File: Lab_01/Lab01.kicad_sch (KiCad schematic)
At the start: 0 parts

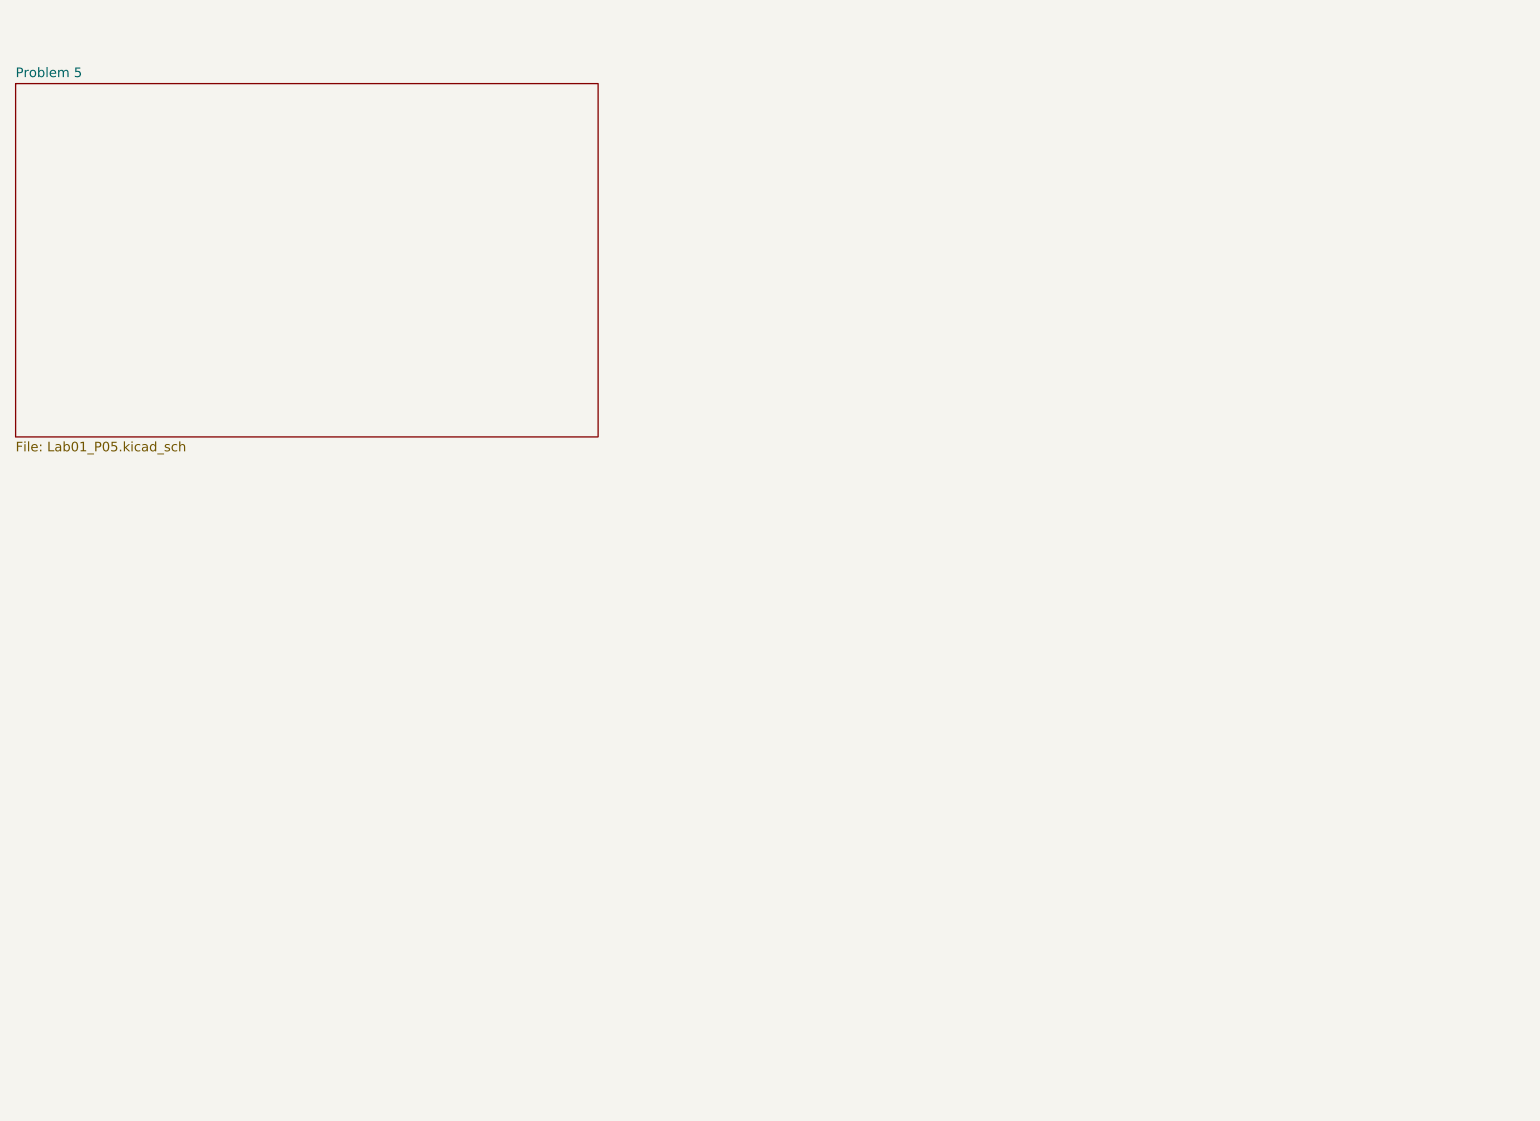
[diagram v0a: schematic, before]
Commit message: Capture and simulate P6&7 schemas
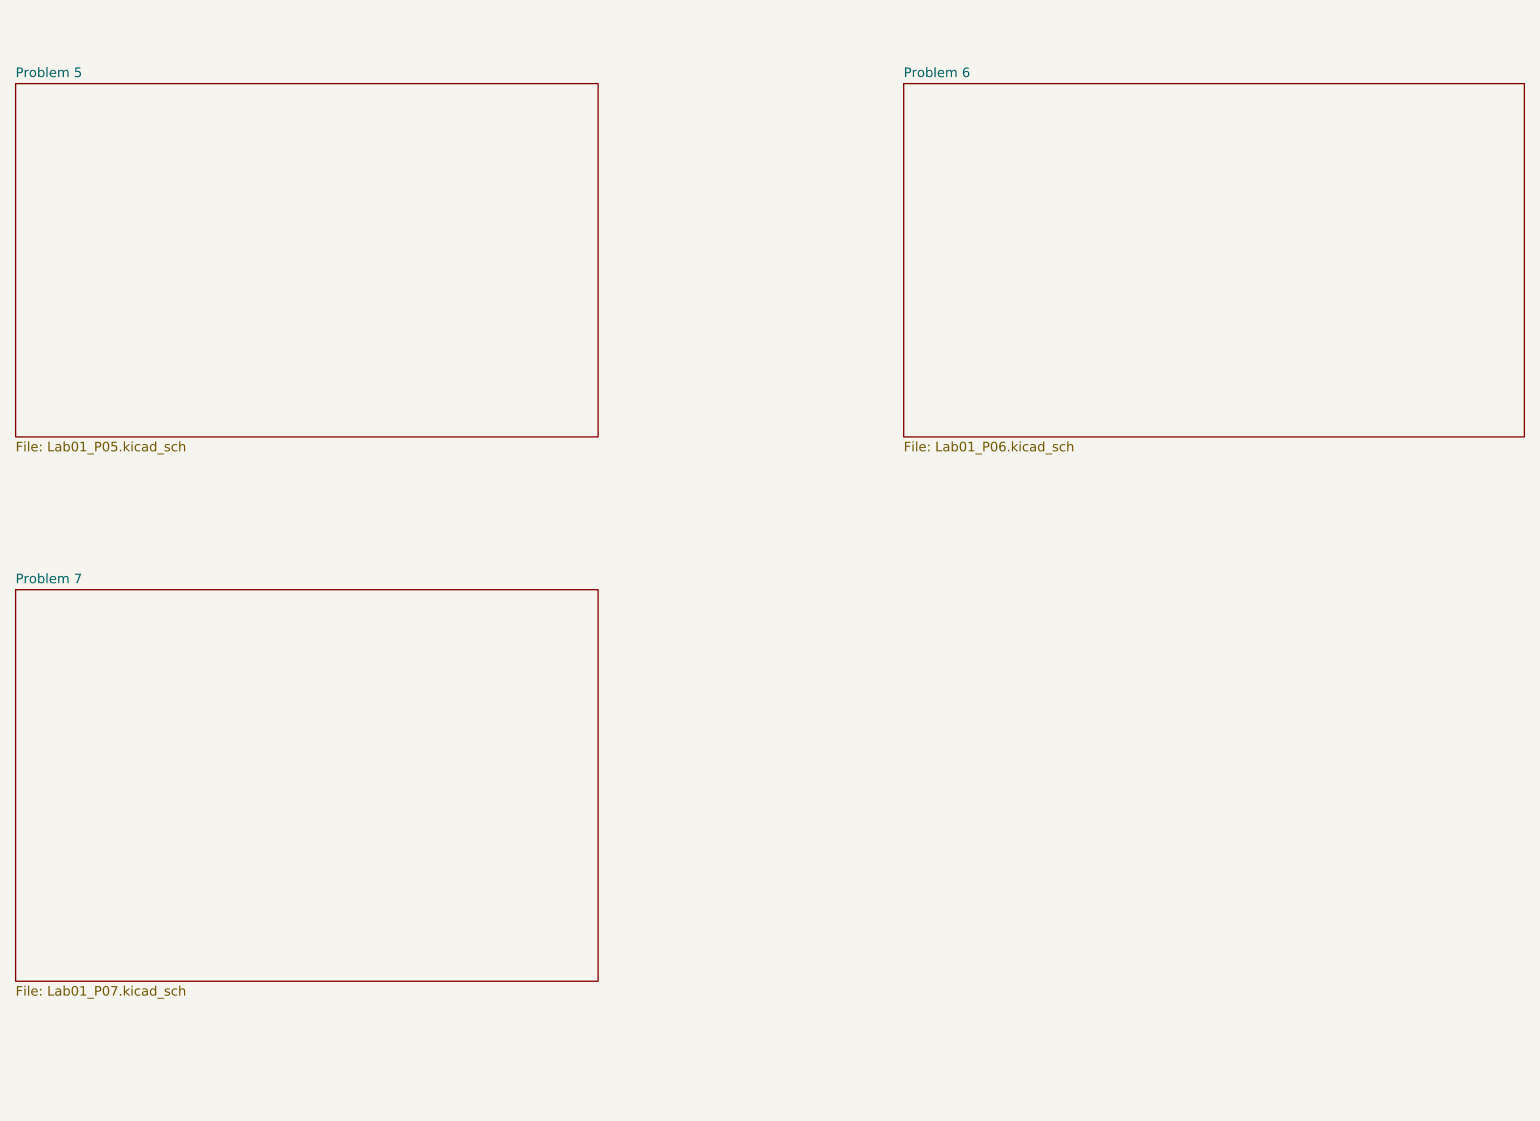
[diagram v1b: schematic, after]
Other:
- added sheet Problem 6 (Lab01_P06.kicad_sch)
- added sheet Problem 7 (Lab01_P07.kicad_sch)
- company: (none) -> Jim Horwitz & Mark Vaughn, Jork Incorporated
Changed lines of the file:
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@@
 (kicad_sch (version 20230121) (generator eeschema)
   (paper "A4")
+  (title_block
+    (date "2024-01-19")
+    (rev "0")
+    (company "Jim Horwitz & Mark Vaughn, Jork Incorporated")
+  )
+  (sheet (at 38.1 99.06) (size 77.47 52.07) (fields_autoplaced)
+    (stroke (width 0.1524) (type solid))
+    (fill (color 0 0 0 0.0000))
+    (property "Sheetname" "Problem 7" (at 38.1 98.3484 0)
+      (effects (font (size 1.27 1.27)) (justify left bottom))
+    )
+    (property "Sheetfile" "Lab01_P07.kicad_sch" (at 38.1 151.7146 0)
+      (effects (font (size 1.27 1.27)) (justify left top))
+    )
+    (instances
+      (project "Lab01"
+        (path "/f5e37932-d66b-45bd-afc2-f24a1a74700d" (page "4"))
+      )
+    )
+  )
   (sheet (at 38.1 31.75) (size 77.47 46.99) (fields_autoplaced)
     (stroke (width 0.1524) (type solid))
@@
       )
     )
+  )
+  (sheet (at 156.21 31.75) (size 82.55 46.99) (fields_autoplaced)
+    (stroke (width 0.1524) (type solid))
+    (fill (color 0 0 0 0.0000))
+    (property "Sheetname" "Problem 6" (at 156.21 31.0384 0)
+      (effects (font (size 1.27 1.27)) (justify left bottom))
+    )
+    (property "Sheetfile" "Lab01_P06.kicad_sch" (at 156.21 79.3246 0)
+      (effects (font (size 1.27 1.27)) (justify left top))
+    )
+    (instances
+      (project "Lab01"
+        (path "/f5e37932-d66b-45bd-afc2-f24a1a74700d" (page "3"))
+      )
+    )

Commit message: Edit up to Question 9
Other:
- added sheet Problem 8 (Lab01_P08.kicad_sch)
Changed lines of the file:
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@@
     (company "Jim Horwitz & Mark Vaughn, Jork Incorporated")
   )
-  (sheet (at 38.1 99.06) (size 77.47 52.07) (fields_autoplaced)
+  (sheet (at 38.1 101.6) (size 38.1 25.4) (fields_autoplaced)
     (stroke (width 0.1524) (type solid))
     (fill (color 0 0 0 0.0000))
-    (property "Sheetname" "Problem 7" (at 38.1 98.3484 0)
+    (property "Sheetname" "Problem 7" (at 38.1 100.8884 0)
       (effects (font (size 1.27 1.27)) (justify left bottom))
     )
-    (property "Sheetfile" "Lab01_P07.kicad_sch" (at 38.1 151.7146 0)
+    (property "Sheetfile" "Lab01_P07.kicad_sch" (at 38.1 127.5846 0)
       (effects (font (size 1.27 1.27)) (justify left top))
     )
@@
     )
   )
-  (sheet (at 38.1 31.75) (size 77.47 46.99) (fields_autoplaced)
+  (sheet (at 38.1 139.7) (size 38.1 25.4) (fields_autoplaced)
     (stroke (width 0.1524) (type solid))
     (fill (color 0 0 0 0.0000))
-    (property "Sheetname" "Problem 5" (at 38.1 31.0384 0)
+    (property "Sheetname" "Problem 8" (at 38.1 138.9884 0)
       (effects (font (size 1.27 1.27)) (justify left bottom))
     )
-    (property "Sheetfile" "Lab01_P05.kicad_sch" (at 38.1 79.3246 0)
+    (property "Sheetfile" "Lab01_P08.kicad_sch" (at 38.1 165.6846 0)
+      (effects (font (size 1.27 1.27)) (justify left top))
+    )
+    (instances
+      (project "Lab01"
+        (path "/f5e37932-d66b-45bd-afc2-f24a1a74700d" (page "5"))
+      )
+    )
+  )
+  (sheet (at 38.1 25.4) (size 38.1 25.4) (fields_autoplaced)
+    (stroke (width 0.1524) (type solid))
+    (fill (color 0 0 0 0.0000))
+    (property "Sheetname" "Problem 5" (at 38.1 24.6884 0)
+      (effects (font (size 1.27 1.27)) (justify left bottom))
+    )
+    (property "Sheetfile" "Lab01_P05.kicad_sch" (at 38.1 51.3846 0)
       (effects (font (size 1.27 1.27)) (justify left top))
     )
@@
     )
   )
-  (sheet (at 156.21 31.75) (size 82.55 46.99) (fields_autoplaced)
+  (sheet (at 38.1 63.5) (size 38.1 25.4) (fields_autoplaced)
     (stroke (width 0.1524) (type solid))
     (fill (color 0 0 0 0.0000))
-    (property "Sheetname" "Problem 6" (at 156.21 31.0384 0)
+    (property "Sheetname" "Problem 6" (at 38.1 62.7884 0)
       (effects (font (size 1.27 1.27)) (justify left bottom))
     )
-    (property "Sheetfile" "Lab01_P06.kicad_sch" (at 156.21 79.3246 0)
+    (property "Sheetfile" "Lab01_P06.kicad_sch" (at 38.1 89.4846 0)
       (effects (font (size 1.27 1.27)) (justify left top))
     )

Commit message: Finish Lab 01
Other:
- added sheet Problem 10 (Lab01_P10.kicad_sch)
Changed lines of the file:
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@@
+    )
+  )
+  (sheet (at 127 63.5) (size 38.1 25.4) (fields_autoplaced)
+    (stroke (width 0.1524) (type solid))
+    (fill (color 0 0 0 0.0000))
+    (property "Sheetname" "Problem 10" (at 127 62.7884 0)
+      (effects (font (size 1.27 1.27)) (justify left bottom))
+    )
+    (property "Sheetfile" "Lab01_P10.kicad_sch" (at 127 89.4846 0)
+      (effects (font (size 1.27 1.27)) (justify left top))
+    )
+    (instances
+      (project "Lab01"
+        (path "/f5e37932-d66b-45bd-afc2-f24a1a74700d" (page "6"))
+      )
     )
   )
